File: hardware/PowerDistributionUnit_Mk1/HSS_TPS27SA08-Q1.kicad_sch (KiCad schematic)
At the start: 29 parts, among them U3 TPS27SA08CQPWPRQ1, U32 ACS37042KLHBLT-010B3

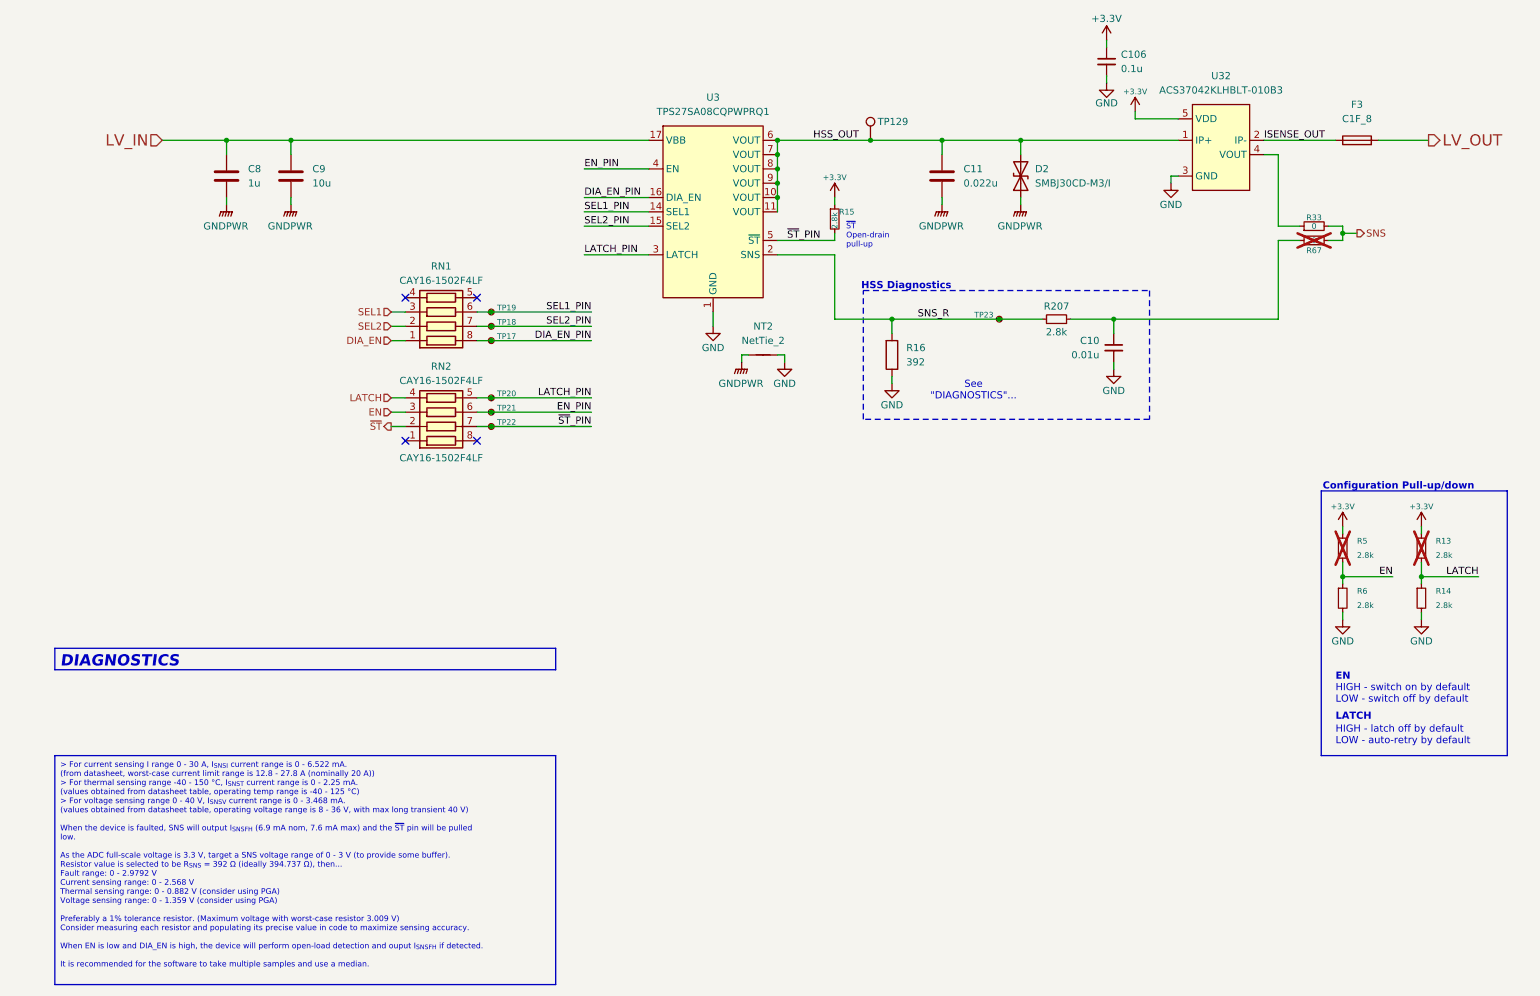
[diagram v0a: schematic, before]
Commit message: BBPDU Mk1 RevB (#6)
* update adc reference to use internal reference (open) with jumper option

* change ADC - reading voltage to resistor divider with option to reference to GND or 1.65V

* change ADC AVDD and AGND connections to regular 3.3V and GND

* make input protection use b2b FETs

* update KiCad-Sharepoint

* update LeaderSOM symbol and SPI pinout (bottom) - need to swap SPI2 and SPI3 names, remove local library copy of LeaderSOM symbol

* change LSOM footprint to centered LSOM footprint, make centered LSOM footprint plated to address hidden pins on LSOM symbol

* update PCB from schematic

* layout/routing for input protection

* fix centered LSOM footprint 3D model, update footprint

* reroute LSOM SPI connections, repin logic analyzer connections

* reroute updated AVDD and AGND on ADCs

* reroute ADCIN- connections to resistor divider from 3.3VA (for 1.65V or 0V)

* change jumper to DNP resistor for ADC reference, routed

* route a couple of missed connections (LV in connection to input prot IC, LV sense connection)

* address DRC

* fix silkscreen labelling issues

* add SRCLK_ENed connection to logic analyzer connector

* silkscreen fixes and stuff

* update rev and year label

* address DRC

* update schematic documentation, clean up, update titleblocks

* add LCSC P/N to libs

* update all symbols with LCSC P/N

* update PCB with LCSC P/Ns

* add center mounting hole

* correct SR part number to SOIC package

* correct fuse table

* change lv sense rdiv values to avoid extended components, update all pull-ups/-downs using 2.8k

* rotate nanofits for inwards clip

* NC the mounting holes (because Lakshay Gupta)

* fix shorted nets error from wrong size res symbol from resistor change

* address DRC

* assembly setup, change latch pull resistor DNP to latch off instead of auto retry by default

* silkscreen stuff

* change DNP for HSS diagnostics to default to current

* change DNP to disable HSS diagnostics by default (primarily use external current 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
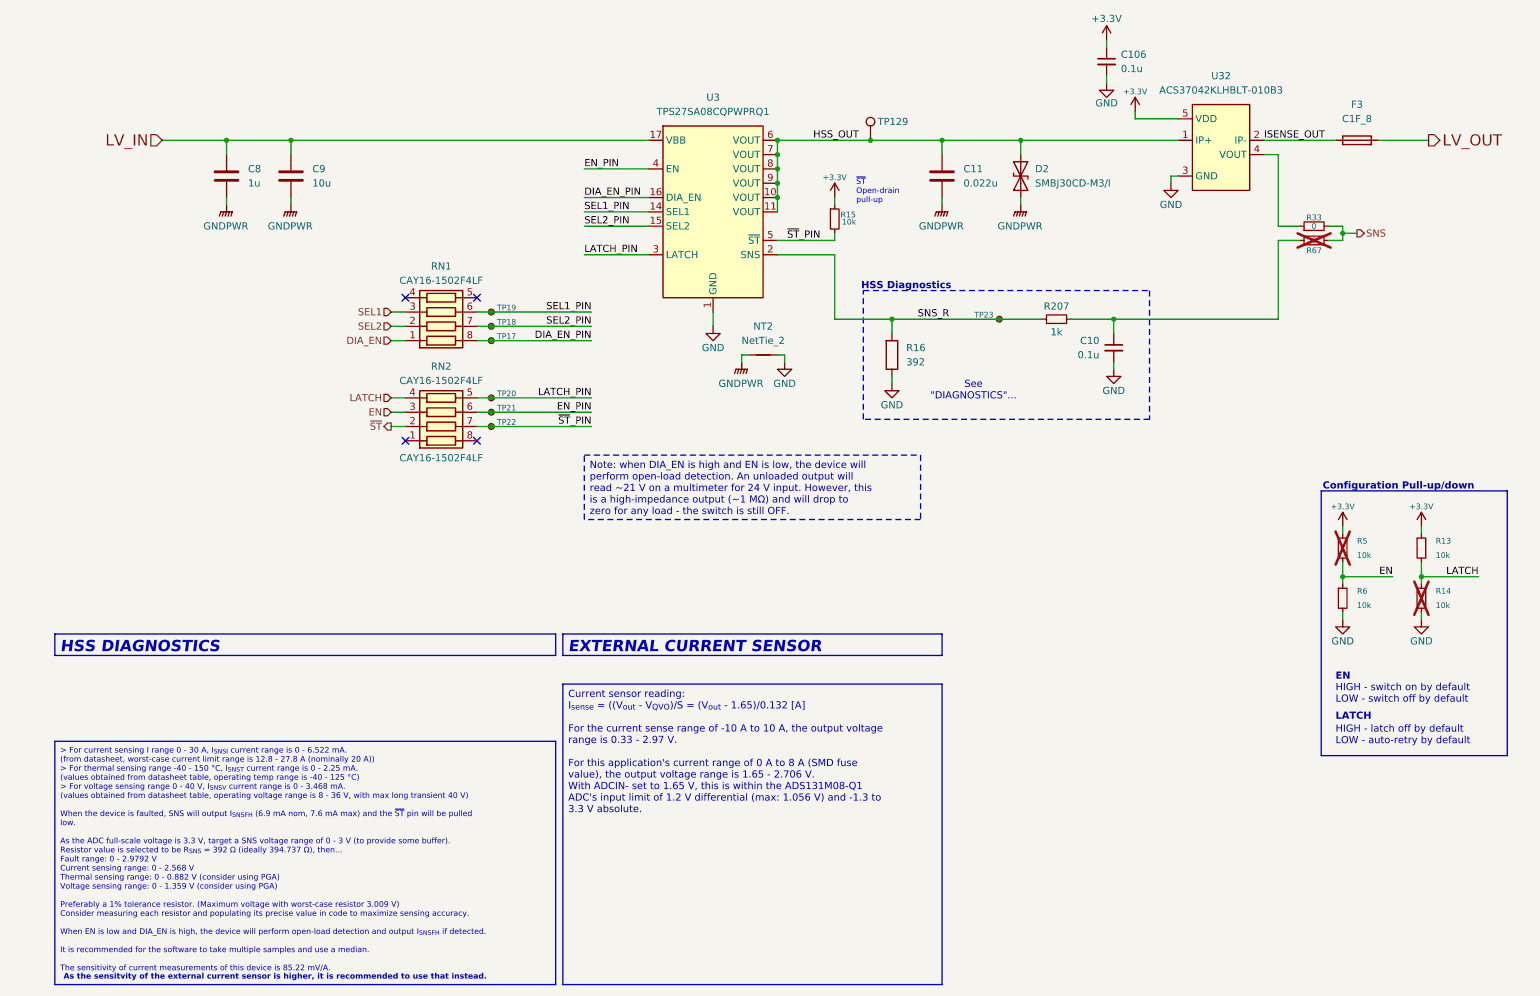
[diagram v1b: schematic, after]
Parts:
- C10: value 0.01u -> 0.1u; symbol PowerDistributionUnitCapacitorLib:0.01u_Small -> PowerDistributionUnitCapacitorLib:0.1u_Small; LCSC P/N (none) -> C14663; Mouser P/N 963-MSASH168SB5103KT -> 963-MLASH168SB7104KT; P/N MSASH168SB5103KTNA01 -> MLASH168SB7104KTNA01
- C106: LCSC P/N (none) -> C14663
- C11: LCSC P/N (none) -> C21122
- C8: LCSC P/N (none) -> C15849
- C9: LCSC P/N (none) -> C440198
- D2: LCSC P/N (none) -> C1973846
- F3: LCSC P/N (none) -> C3162293
- R13: value 2.8k -> 10k; symbol PowerDistributionUnitResistorLib:2.8k_Small -> PowerDistributionUnitResistorLib:10k_Small; LCSC P/N (none) -> C25804; Mouser P/N 71-CRCW0603-2.8K-E3 -> 71-CRCW060310K0FKEI; P/N CRCW06032K80FKEA -> CRCW060310K0FKEI; now fitted
- R14: value 2.8k -> 10k; symbol PowerDistributionUnitResistorLib:2.8k_Small -> PowerDistributionUnitResistorLib:10k_Small; LCSC P/N (none) -> C25804; Mouser P/N 71-CRCW0603-2.8K-E3 -> 71-CRCW060310K0FKEI; P/N CRCW06032K80FKEA -> CRCW060310K0FKEI; now not fitted
- R15, R5, R6: value 2.8k -> 10k; symbol PowerDistributionUnitResistorLib:2.8k_Small -> PowerDistributionUnitResistorLib:10k_Small; LCSC P/N (none) -> C25804; Mouser P/N 71-CRCW0603-2.8K-E3 -> 71-CRCW060310K0FKEI; P/N CRCW06032K80FKEA -> CRCW060310K0FKEI
- R16: LCSC P/N (none) -> C245964
- R207: value 2.8k -> 1k; symbol PowerDistributionUnitResistorLib:2.8k_Small -> PowerDistributionUnitResistorLib:1k_Small; Digikey P/N 541-2.80KHCT-ND -> 541-CRCW06031K00FKEECT-ND; LCSC P/N (none) -> C21190; Mouser P/N 71-CRCW0603-2.8K-E3 -> 71-CRCW06031K00FKEI; P/N CRCW06032K80FKEA -> CRCW06031K00FKEI
- R33, R67: LCSC P/N (none) -> C21189
- RN1, RN2: Alt LCSC P/N (none) -> C25728; LCSC P/N (none) -> C5590111
- U3: LCSC P/N (none) -> C2870129
- U32: LCSC P/N (none) -> C45176726
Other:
- note added: "As the sensitvity of the external current sensor is higher, it is recommended to use that instead."
